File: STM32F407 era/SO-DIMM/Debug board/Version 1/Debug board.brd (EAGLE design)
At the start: 91.4 x 33.3 mm, 10 parts, among them J4 FTDI_DEVICE, X1 057-014-1, X2 BN35N61, X3 BN35N61, X4 BN35N61, X5 BN35N61, X6 BN35N61

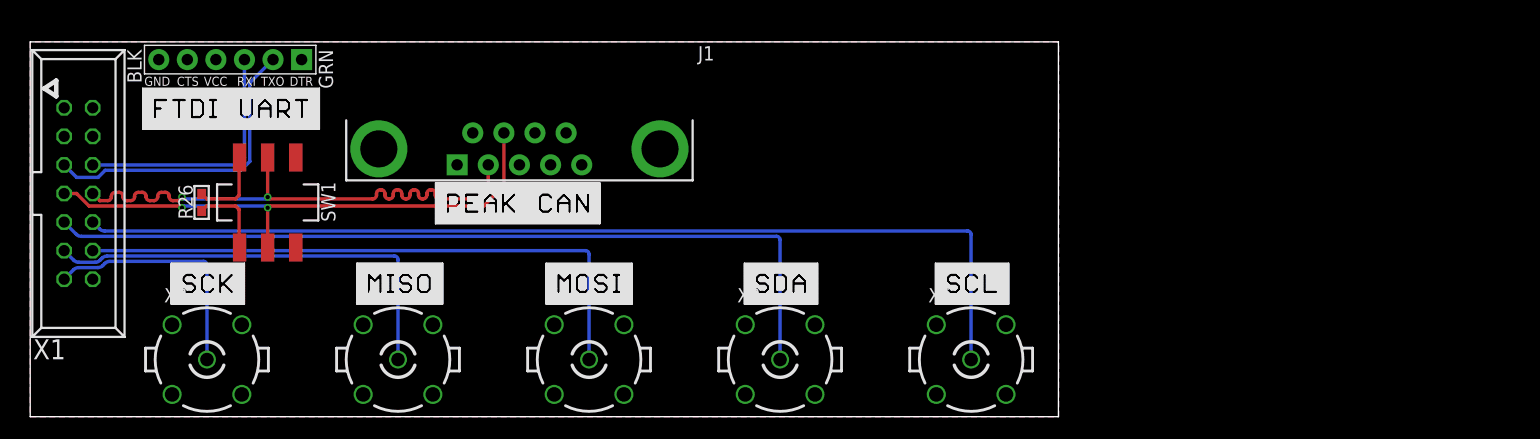
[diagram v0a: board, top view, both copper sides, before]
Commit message: more work on debug board silkscreen
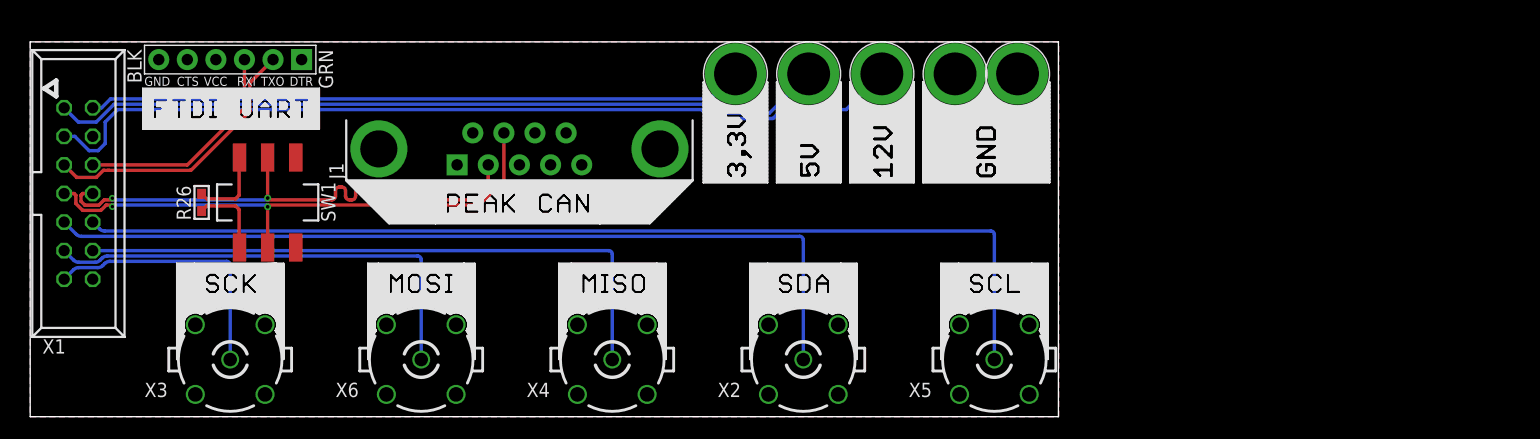
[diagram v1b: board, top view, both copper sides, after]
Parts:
- added J2, J3, J5, J6, J7: (no value), SparkFun-Connectors:BANANA_CONN
- R26: value 60 -> 120
- moved X3 2.06 mm to (17.6, 13.3)
- moved X2 2.06 mm to (68.6, 13.3)
- moved X4 2.06 mm to (51.6, 13.3)
- moved X5 2.06 mm to (85.6, 13.3)
- moved X6 2.06 mm to (34.6, 13.3)
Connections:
- net CANH renamed CAN_P
- net CANL renamed CAN_N
- net 12V: now also J5.P$1
- net 3.3V: now also J2.P$1
- net 5.0V: now also J3.P$1
- net GND: now also J6.P$1, J7.P$1
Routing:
- net 12V: track 0.00 -> 77.8 mm
- net 5.0V: track 0.00 -> 69.2 mm
- net 3.3V: track 0.00 -> 58.4 mm
- net DBG_TX: track 27.5 -> 24.9 mm
- net DBG_RX: track 22.5 -> 19.9 mm
- net CAN_N: track 47.3 -> 49.5 mm
- net SCK: track 21.8 -> 23.8 mm
- net SDA: track 74.9 -> 77.0 mm
- net SCL: track 89.6 -> 91.7 mm
- net MOSI: track 39.2 -> 41.3 mm
- net MISO: track 53.6 -> 55.7 mm
- net CAN_P: track 48.8 -> 50.7 mm

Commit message: added 12V aux power to debug board
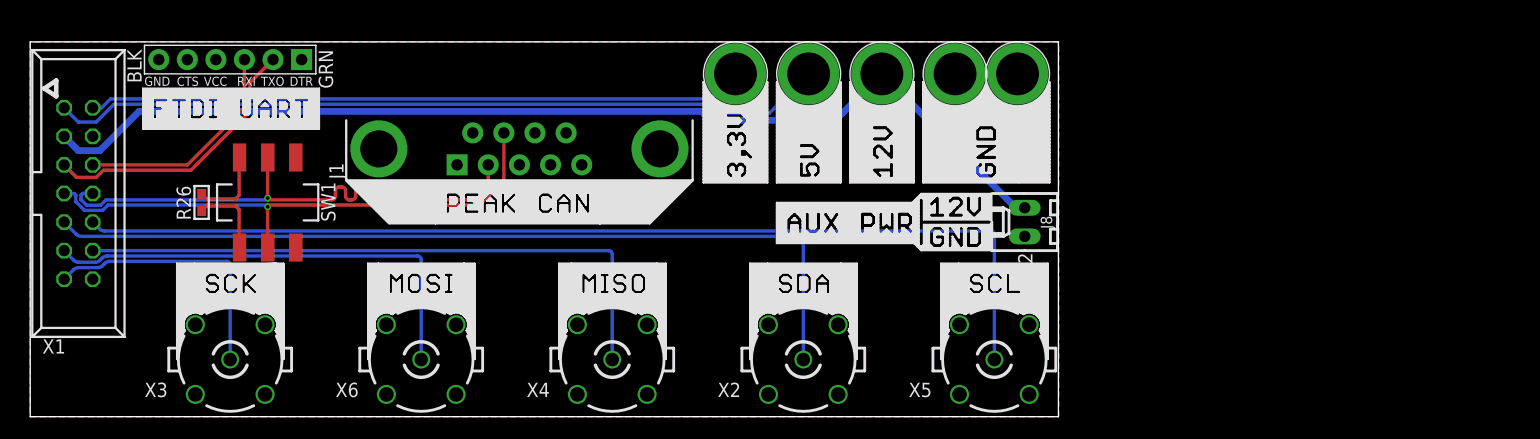
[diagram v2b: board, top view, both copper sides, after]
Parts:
- added J8: 22-27-2021-02, con-molex:6410-02
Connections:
- net 12V: now also J8.1
- net GND: now also J8.2
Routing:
- net 12V: track 77.8 -> 94.4 mm
- net CAN_P: track 50.7 -> 50.3 mm, vias 2 -> 1
- net CAN_N: track 49.5 -> 49.1 mm, vias 2 -> 1

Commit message: USB to UART done, mork work on COM/TC
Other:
- board text added: "Debug board Version 1"

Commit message: All board V1-RC1 done
all boards ready for inspection
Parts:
- added U$21: MICROFIT4, unicorn:43045-0400
- added U5, U6: (no value), connector:AUDIO-JACK
- added X7, X8: BN35N61, con-coax:B35N61
- moved J7 37.9 mm to (125.6, 38.6)
- moved J2 37.9 mm to (100.5, 38.6)
- moved J3 37.9 mm to (107.0, 38.6)
- moved J5 37.9 mm to (113.5, 38.6)
- moved J6 37.9 mm to (120.0, 38.6)
- moved J8 37.3 mm to (125.6, 26.0)
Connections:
- net CAN_N: now also U$21.P$3, U5.TIP, U6.TIP, X7.1
- net CAN_P: now also U$21.P$4, U5.RING, U6.RING, X8.1
- net GND: now also U$21.P$1, U$21.P$2, U5.SLEEVE, U6.SLEEVE, X7.2, X7.3, X7.4, X7.5, X8.2, X8.3, X8.4, X8.5
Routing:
- net CAN_N: track 49.1 -> 172.2 mm, vias 1 -> 4
- net CAN_P: track 50.3 -> 171.2 mm, vias 1 -> 4
- net 3.3V: track 58.4 -> 107.5 mm, vias 0 -> 2
- net 5.0V: track 69.2 -> 115.1 mm, vias 0 -> 2
- net 12V: track 94.4 -> 137.0 mm
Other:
- board size 91.4 x 33.3 mm -> 128.9 x 33.3 mm

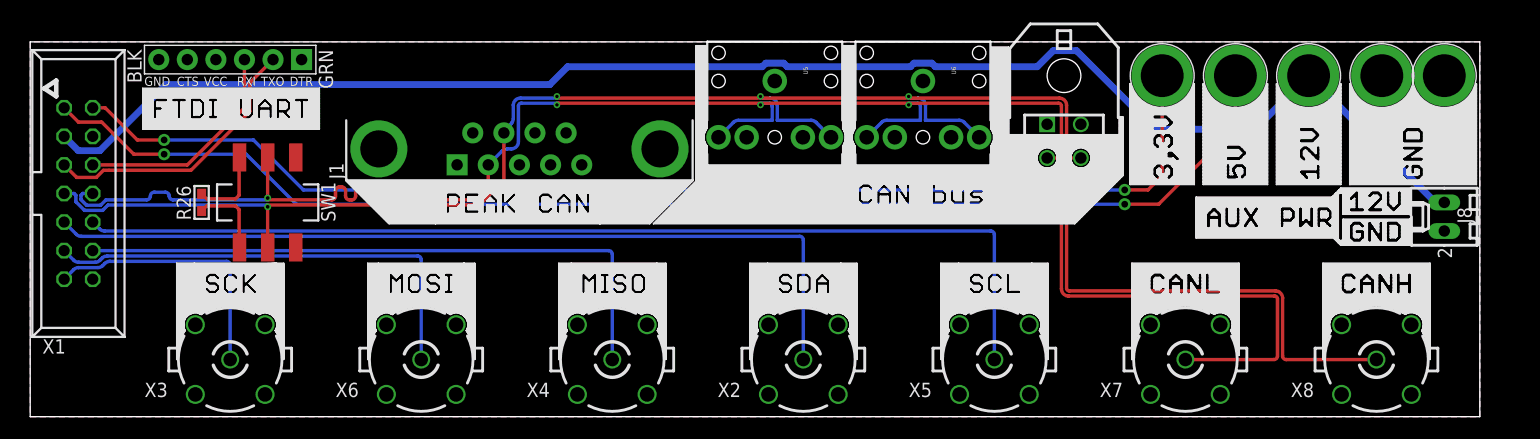
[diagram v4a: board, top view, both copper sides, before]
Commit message: last end changes on boards
Dev board
- Added 8 LED for ekstra debugging feature
- fixed Tvalue silkscreen
-

COM/TC
- fixed connections om P-channel RPP
- 12V from debug changed to include RPP and fuse

Dash
- fixed connections om P-channel RPP
- 12V from debug changed to include RPP and fuse

debug
- Added "ohm/not ohm to silkscreen
- Added BNC connectors for CAN

and much much more
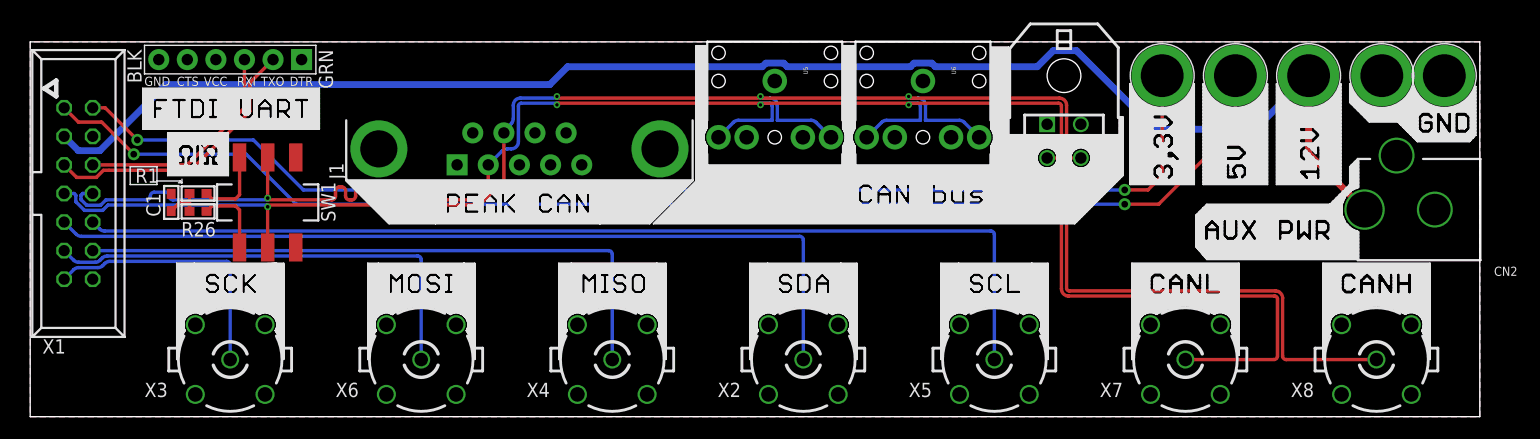
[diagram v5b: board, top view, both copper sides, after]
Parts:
- removed J8: 22-27-2021-02, con-molex:6410-02
- added C1: 47n, microbuilder:_0603
- added CN2: (no value), microbuilder:DCJACK_2MM_PTH
- added R1: 60, microbuilder:_0603
- R26: value 120 -> 60
- moved R26 0.85 mm to (14.8, 26.5), turned to 0 degrees
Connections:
- removed net N$8: R26.1, SW1.P$3
- new net N$1: C1.1, R1.2, R26.1
- new net N$2: R1.1, SW1.P$3
- net 12V: now also CN2.PWR; no longer J8.1
- net GND: now also C1.2, CN2.GND, CN2.GNDBREAK; no longer J8.2
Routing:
- net N$8: track 7.03 -> 0.00 mm
- net N$2: track 0.00 -> 6.60 mm
- net N$1: track 0.00 -> 3.52 mm
- net 12V: track 137.0 -> 134.2 mm
